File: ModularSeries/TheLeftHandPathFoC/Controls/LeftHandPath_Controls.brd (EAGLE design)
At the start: 48.5 x 100 mm, 14 parts, among them SW1 SPDT_SWITCHDW1

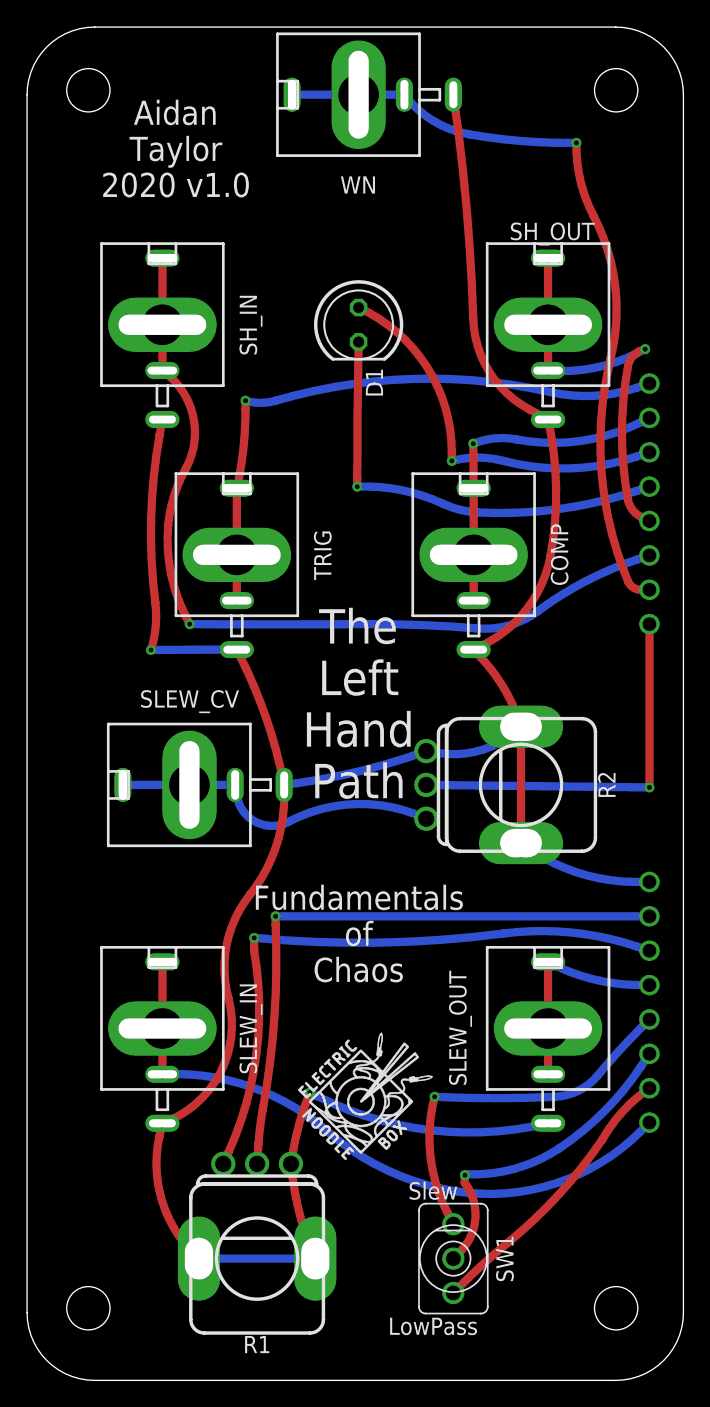
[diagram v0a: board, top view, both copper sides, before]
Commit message: Portals BOM update, Ffrydiau project added
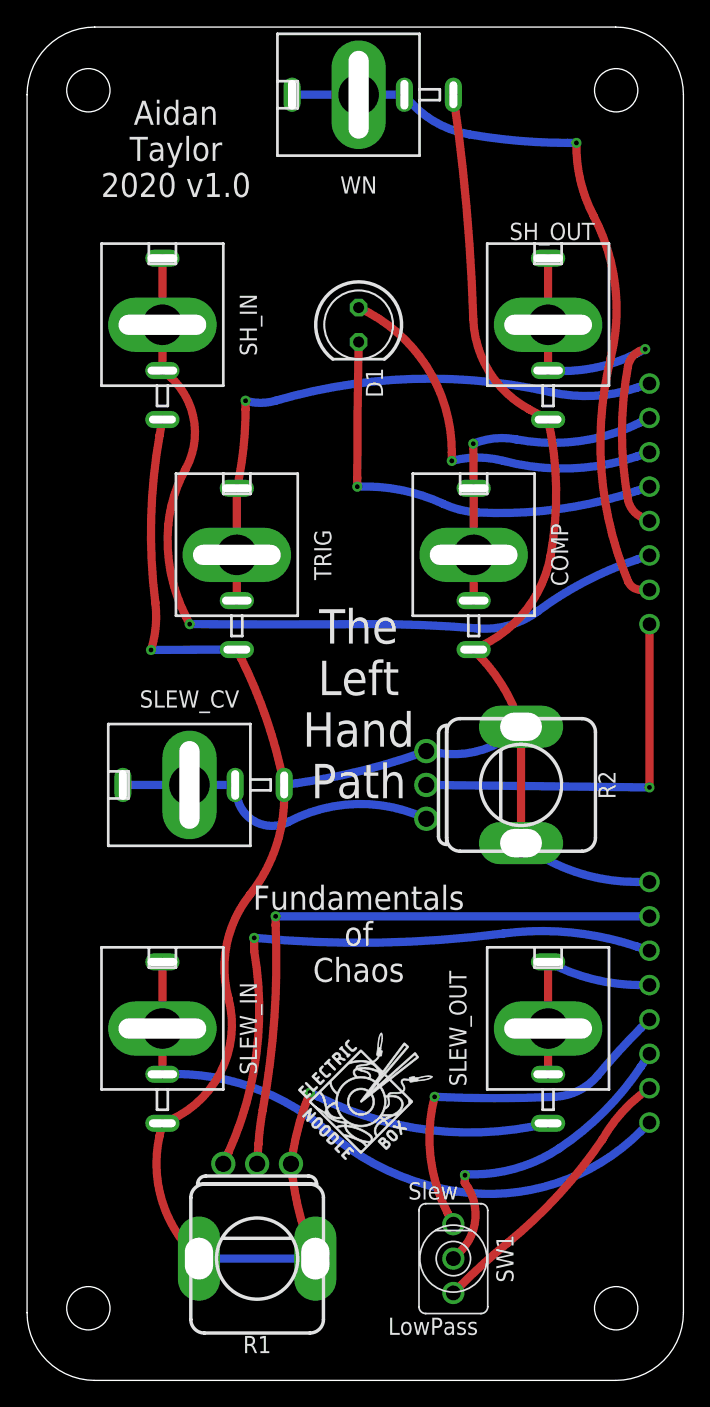
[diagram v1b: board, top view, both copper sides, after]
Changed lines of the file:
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@@
 </layers>
 <board>
+<fusionsync huburn="a.cGVyc29uYWw6dWUyYjdlNGE0" projecturn="a.cGVyc29uYWw6dWUyYjdlNGE0IzIwMjAwNDA1MjgzMzA0MTgx" f3durn="urn:adsk.wipprod:dm.lineage:kmEMbdZuTkq2Sp1QK2xSPA" pcbguid="" lastpulledtime="" lastsyncedchangeguid="" latestrevisionid="01dfa6b5-5bf5-4181-b1f7-78773aa01459" lastsyncedrevisionid="01dfa6b5-5bf5-4181-b1f7-78773aa01459" lastboardhashguid="ae33d621-d120-0d73-d84d-287dbf57df36" lastpushedtime="2020-07-13T08:11:04Z" linktopcb3d="true"/>
 <plain>
 <text x="25.5" y="50" size="2.54" layer="21" font="vector" ratio="16" align="center">The
@@
 2020 v1.0</text>
 <wire x1="0" y1="-14.25" x2="50.5" y2="-14.25" width="0.6096" layer="49"/>
-<wire x1="50.5" y1="-14.25" x2="50.5" y2="-9.25" width="0.6096" layer="49"/>
-<wire x1="50.5" y1="109.25" x2="50.5" y2="114.25" width="0.6096" layer="49"/>
+<wire x1="50.5" y1="-14.25" x2="50.5" y2="-8.25" width="0.6096" layer="49"/>
+<wire x1="50.5" y1="108.25" x2="50.5" y2="114.25" width="0.6096" layer="49"/>
 <wire x1="50.5" y1="114.25" x2="0" y2="114.25" width="0.6096" layer="49"/>
-<wire x1="0" y1="114.25" x2="0" y2="109.25" width="0.6096" layer="49"/>
-<wire x1="0" y1="-9.25" x2="0" y2="-14.25" width="0.6096" layer="49"/>
+<wire x1="0" y1="114.25" x2="0" y2="108.25" width="0.6096" layer="49"/>
+<wire x1="0" y1="-8.25" x2="0" y2="-14.25" width="0.6096" layer="49"/>
 <wire x1="1" y1="95" x2="1" y2="5" width="0" layer="20"/>
 <wire x1="1" y1="5" x2="6" y2="0" width="0" layer="20" curve="90"/>
@@
 <wire x1="44.5" y1="100" x2="6" y2="100" width="0" layer="20"/>
 <wire x1="6" y1="100" x2="1" y2="95" width="0" layer="20" curve="90"/>
-<wire x1="0" y1="-9.25" x2="50.5" y2="-9.25" width="0.6096" layer="49"/>
-<wire x1="50.5" y1="-9.25" x2="50.5" y2="109.25" width="0.6096" layer="49"/>
-<wire x1="50.5" y1="109.25" x2="0" y2="109.25" width="0.6096" layer="49"/>
-<wire x1="0" y1="109.25" x2="0" y2="-9.25" width="0.6096" layer="49"/>
+<wire x1="0" y1="-8.25" x2="50.5" y2="-8.25" width="0.6096" layer="49"/>
+<wire x1="50.5" y1="-8.25" x2="50.5" y2="108.25" width="0.6096" layer="49"/>
+<wire x1="50.5" y1="108.25" x2="0" y2="108.25" width="0.6096" layer="49"/>
+<wire x1="0" y1="108.25" x2="0" y2="-8.25" width="0.6096" layer="49"/>
 <text x="31" y="4" size="1.27" layer="21" font="vector" ratio="16" align="center">LowPass</text>
 <text x="31" y="14" size="1.27" layer="21" font="vector" ratio="16" align="center">Slew</text>
@@
 </note>
 <note version="8.3" severity="warning">
+Since Version 8.3, EAGLE supports Fusion synchronisation.
+This feature will not be available in this version and saving
+the document will break the link to the Fusion PCB feature.
+</note>
+<note version="8.3" severity="warning">

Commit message: Layout and schematic renders for LHP added
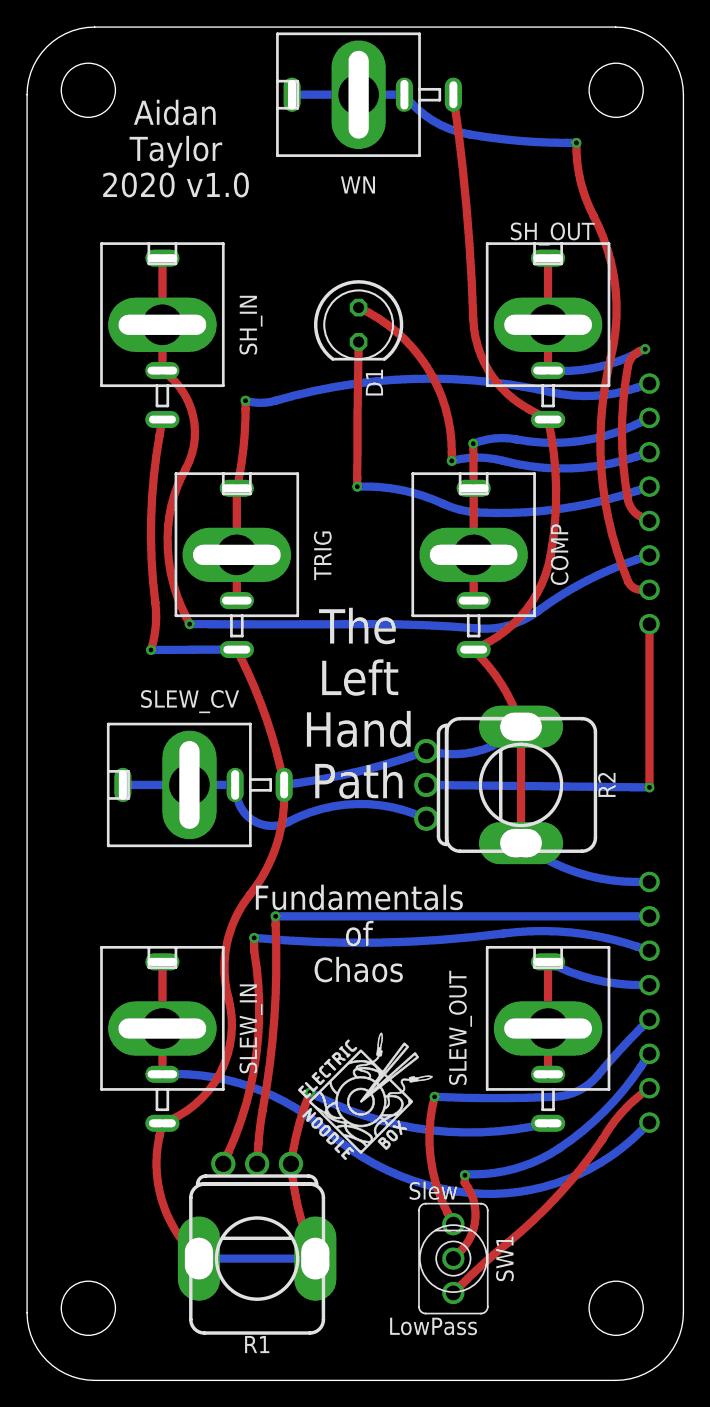
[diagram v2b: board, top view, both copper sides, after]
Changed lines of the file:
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@@
 <layer number="44" name="Drills" color="7" fill="1" visible="no" active="yes"/>
 <layer number="45" name="Holes" color="7" fill="1" visible="no" active="yes"/>
-<layer number="46" name="Milling" color="3" fill="1" visible="no" active="yes"/>
+<layer number="46" name="Milling" color="3" fill="1" visible="yes" active="yes"/>
 <layer number="47" name="Measures" color="7" fill="1" visible="no" active="yes"/>
 <layer number="48" name="Document" color="7" fill="1" visible="no" active="yes"/>
